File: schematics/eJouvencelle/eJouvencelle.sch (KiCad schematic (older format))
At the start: 42 parts

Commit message: reorganise components
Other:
- moved on the sheet: BZ?, C?, J?, Q?, R?, SW?A, U?, Y?

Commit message: convert logic voltage use to 3.3V
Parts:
- removed U?: LM1117IMPX-5.0/NOPB, symbol Regulator_Linear:LM1117-5.0
- added U?: LM1117-3.3, symbol Regulator_Linear:LM1117-3.3
- R? (x7): value 270R -> 100R
- Y?: value 16MHz -> 8MHz
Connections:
- net GND: now also U?.1 (GND)
- net Vbatt: now also U?.3 (VI)
- net +3V3: now reaches J?.2 (Pin_2)
- net +3V3: now also C?.1, C?.1, C?.1, C?.1, C?.1, R?.2, SW?.7 (B), U?.16 (VDD), U?.18 (AVCC), U?.3 (~LT), U?.4 (VCC), U?.6 (VCC), U?.2 (VO)
- removed net +5V: C?.1, C?.1, C?.1, C?.1, C?.1, J?.3 (Pin_3), R?.2, SW?.7 (B), U?.16 (VDD), U?.18 (AVCC), U?.3 (~LT), U?.4 (VCC), U?.6 (VCC)
- no-connect marks 3 -> 11
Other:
- note added: "Voltage regulation (3.3V)"
- note removed: "Voltage regulation (5V)"
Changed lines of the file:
@@
 Sheet 1 1
 Title "eJouvencelle"
-Date "2020-04-04"
+Date "2020-10-03"
 Rev "v3.0"
 Comp ""
@@
 F 3 "" H 5200 5850 50  0001 C CNN
 	1    5200 5850
-	1    0    0    -1
-$EndComp
-$Comp
-L power:+5V #PWR?
-U 1 1 5E88AC5A
-P 5200 2450
-F 0 "#PWR?" H 5200 2300 50  0001 C CNN
-F 1 "+5V" H 5215 2623 50  0000 C CNN
-F 2 "" H 5200 2450 50  0001 C CNN
-F 3 "" H 5200 2450 50  0001 C CNN
-	1    5200 2450
 	1    0    0    -1
 $EndComp
@@
 Connection ~ 5950 2850
 $Comp
-L power:+5V #PWR?
-U 1 1 5E8E172E
-P 2900 3600
-F 0 "#PWR?" H 2900 3450 50  0001 C CNN
-F 1 "+5V" H 2915 3773 50  0000 C CNN
-F 2 "" H 2900 3600 50  0001 C CNN
-F 3 "" H 2900 3600 50  0001 C CNN
-	1    2900 3600
-	1    0    0    -1
-$EndComp
-$Comp
 L power:GND #PWR?
 U 1 1 5E8E3004
@@
 Wire Wire Line
 	2300 3900 2300 4100
-$Comp
-L Regulator_Linear:LM1117-5.0 U?
-U 1 1 5E8E0075
-P 2300 3600
-F 0 "U?" H 2300 3842 50  0000 C CNN
-F 1 "LM1117IMPX-5.0/NOPB" H 2300 3751 50  0000 C CNN
-F 2 "" H 2300 3600 50  0001 C CNN
-F 3 "http://www.ti.com/lit/ds/symlink/lm1117.pdf" H 2300 3600 50  0001 C CNN
-	1    2300 3600
-	1    0    0    -1
-$EndComp
 Text GLabel 1750 3600 0    50   Input ~ 0
 Vbatt
@@
 	1900 4100 2300 4100
 Text Notes 1400 4500 0    50   ~ 0
-Voltage regulation (5V)
+Voltage regulation (3.3V)
 Wire Wire Line
 	2650 3600 2900 3600
@@
 P 4250 4300
 F 0 "Y?" H 4250 4525 50  0000 C CNN
-F 1 "16MHz" H 4250 4434 50  0000 C CNN
+F 1 "8MHz" H 4250 4434 50  0000 C CNN
 F 2 "" H 4250 4300 50  0001 C CNN
 F 3 "~" H 4250 4300 50  0001 C CNN
@@
 $EndComp
 $Comp
-L power:+5V #PWR?
-U 1 1 5E88FEF1
-P 8550 1200
-F 0 "#PWR?" H 8550 1050 50  0001 C CNN
-F 1 "+5V" H 8565 1373 50  0000 C CNN
-F 2 "" H 8550 1200 50  0001 C CNN
-F 3 "" H 8550 1200 50  0001 C CNN
-	1    8550 1200
-	1    0    0    -1
-$EndComp
-$Comp
 L power:GND #PWR?
 U 1 1 5E890F98
@@
 	8550 1250 8550 1450
 $Comp
-L power:+5V #PWR?
-U 1 1 5E89B064
-P 8000 1450
-F 0 "#PWR?" H 8000 1300 50  0001 C CNN
-F 1 "+5V" H 8015 1623 50  0000 C CNN
-F 2 "" H 8000 1450 50  0001 C CNN
-F 3 "" H 8000 1450 50  0001 C CNN
-	1    8000 1450
-	1    0    0    -1
-$EndComp
-$Comp
 L Device:R R?
 U 1 1 5E8C3C3B
 P 9450 1750
 F 0 "R?" V 9400 1850 50  0000 L CNN
-F 1 "270R" V 9400 1450 50  0000 L CNN
+F 1 "100R" V 9400 1450 50  0000 L CNN
 F 2 "" V 9380 1750 50  0001 C CNN
 F 3 "~" H 9450 1750 50  0001 C CNN
@@
 P 9450 1850
 F 0 "R?" V 9400 1950 50  0000 L CNN
-F 1 "270R" V 9400 1550 50  0000 L CNN
+F 1 "100R" V 9400 1550 50  0000 L CNN
 F 2 "" V 9380 1850 50  0001 C CNN
 F 3 "~" H 9450 1850 50  0001 C CNN
@@
 P 9450 1950
 F 0 "R?" V 9400 2050 50  0000 L CNN
-F 1 "270R" V 9400 1650 50  0000 L CNN
+F 1 "100R" V 9400 1650 50  0000 L CNN
 F 2 "" V 9380 1950 50  0001 C CNN
 F 3 "~" H 9450 1950 50  0001 C CNN
@@
 P 9450 2050
 F 0 "R?" V 9400 2150 50  0000 L CNN
-F 1 "270R" V 9400 1750 50  0000 L CNN
+F 1 "100R" V 9400 1750 50  0000 L CNN
 F 2 "" V 9380 2050 50  0001 C CNN
 F 3 "~" H 9450 2050 50  0001 C CNN
@@
 P 9450 2150
 F 0 "R?" V 9400 2250 50  0000 L CNN
-F 1 "270R" V 9400 1850 50  0000 L CNN
+F 1 "100R" V 9400 1850 50  0000 L CNN
 F 2 "" V 9380 2150 50  0001 C CNN
 F 3 "~" H 9450 2150 50  0001 C CNN
@@
 P 9450 2250
 F 0 "R?" V 9400 2350 50  0000 L CNN
-F 1 "270R" V 9400 1950 50  0000 L CNN
+F 1 "100R" V 9400 1950 50  0000 L CNN
 F 2 "" V 9380 2250 50  0001 C CNN
 F 3 "~" H 9450 2250 50  0001 C CNN
@@
 P 9450 2350
 F 0 "R?" V 9400 2450 50  0000 L CNN
-F 1 "270R" V 9400 2050 50  0000 L CNN
+F 1 "100R" V 9400 2050 50  0000 L CNN
 F 2 "" V 9380 2350 50  0001 C CNN
 F 3 "~" H 9450 2350 50  0001 C CNN
@@
 	9650 4000 9650 4050
 $Comp
-L power:+5V #PWR?
-U 1 1 5E933D66
-P 9650 3700
-F 0 "#PWR?" H 9650 3550 50  0001 C CNN
-F 1 "+5V" H 9665 3873 50  0000 C CNN
-F 2 "" H 9650 3700 50  0001 C CNN
-F 3 "" H 9650 3700 50  0001 C CNN
-	1    9650 3700
-	-1   0    0    -1
-$EndComp
-$Comp
 L Device:R R?
 U 1 1 5E9329C4
@@
 Wire Wire Line
 	10150 4250 10300 4250
-Wire Wire Line
-	10000 4450 10300 4450
-Wire Wire Line
-	10000 4500 10000 4450
 Wire Wire Line
 	10200 4650 10300 4650
@@
 $EndComp
 $Comp
-L power:+5V #PWR?
-U 1 1 5E917405
-P 10000 4500
-F 0 "#PWR?" H 10000 4350 50  0001 C CNN
-F 1 "+5V" H 10015 4673 50  0000 C CNN
-F 2 "" H 10000 4500 50  0001 C CNN
-F 3 "" H 10000 4500 50  0001 C CNN
-	1    10000 4500
-	1    0    0    1
-$EndComp
-NoConn ~ 10300 4550
-$Comp
 L power:GND #PWR?
 U 1 1 5E9155DD
@@
 Wire Wire Line
 	2000 1500 2000 1550
-$Comp
-L power:+5V #PWR?
-U 1 1 5E8B2017
-P 2000 1500
-F 0 "#PWR?" H 2000 1350 50  0001 C CNN
-F 1 "+5V" H 2015 1673 50  0000 C CNN
-F 2 "" H 2000 1500 50  0001 C CNN
-F 3 "" H 2000 1500 50  0001 C CNN
-	1    2000 1500
-	1    0    0    -1
-$EndComp
 Connection ~ 2750 1000
 Wire Wire Line
@@
 Wire Wire Line
 	5800 3700 7550 3700
+$Comp
+L power:+3V3 #PWR?
+U 1 1 5F79539F
+P 2900 3600
+F 0 "#PWR?" H 2900 3450 50  0001 C CNN
+F 1 "+3V3" H 2915 3773 50  0000 C CNN
+F 2 "" H 2900 3600 50  0001 C CNN
+F 3 "" H 2900 3600 50  0001 C CNN
+	1    2900 3600
+	1    0    0    -1
+$EndComp
+$Comp
+L power:+3V3 #PWR?
+U 1 1 5F795FB2
+P 2000 1500
+F 0 "#PWR?" H 2000 1350 50  0001 C CNN
+F 1 "+3V3" H 2015 1673 50  0000 C CNN
+F 2 "" H 2000 1500 50  0001 C CNN
+F 3 "" H 2000 1500 50  0001 C CNN
+	1    2000 1500
+	1    0    0    -1
+$EndComp
+$Comp
+L power:+3V3 #PWR?
+U 1 1 5F797225
+P 5200 2450
+F 0 "#PWR?" H 5200 2300 50  0001 C CNN
+F 1 "+3V3" H 5215 2623 50  0000 C CNN
+F 2 "" H 5200 2450 50  0001 C CNN
+F 3 "" H 5200 2450 50  0001 C CNN
+	1    5200 2450
+	1    0    0    -1
+$EndComp
+$Comp
+L power:+3V3 #PWR?
+U 1 1 5F7984BD
+P 8550 1200
+F 0 "#PWR?" H 8550 1050 50  0001 C CNN
+F 1 "+3V3" H 8565 1373 50  0000 C CNN
+F 2 "" H 8550 1200 50  0001 C CNN
+F 3 "" H 8550 1200 50  0001 C CNN
+	1    8550 1200
+	1    0    0    -1
+$EndComp
+$Comp
+L power:+3V3 #PWR?
+U 1 1 5F799711
+P 8000 1450
+F 0 "#PWR?" H 8000 1300 50  0001 C CNN
+F 1 "+3V3" H 8015 1623 50  0000 C CNN
+F 2 "" H 8000 1450 50  0001 C CNN
+F 3 "" H 8000 1450 50  0001 C CNN
+	1    8000 1450
+	1    0    0    -1
+$EndComp
+$Comp
+L power:+3V3 #PWR?
+U 1 1 5F79A562
+P 9650 3700
+F 0 "#PWR?" H 9650 3550 50  0001 C CNN
+F 1 "+3V3" H 9665 3873 50  0000 C CNN
+F 2 "" H 9650 3700 50  0001 C CNN
+F 3 "" H 9650 3700 50  0001 C CNN
+	1    9650 3700
+	1    0    0    -1
+$EndComp
+$Comp
+L power:+3V3 #PWR?
+U 1 1 5F7ACFC0
+P 10050 4600
+F 0 "#PWR?" H 10050 4450 50  0001 C CNN
+F 1 "+3V3" H 10065 4773 50  0000 C CNN
+F 2 "" H 10050 4600 50  0001 C CNN
+F 3 "" H 10050 4600 50  0001 C CNN
+	1    10050 4600
+	-1   0    0    1
+$EndComp
+Wire Wire Line
+	10300 4550 10050 4550
+Wire Wire Line
+	10050 4550 10050 4600
+NoConn ~ 10300 4450
+NoConn ~ 4600 3350
+NoConn ~ 4600 3450
+NoConn ~ 4600 5350
+NoConn ~ 4600 5450
+NoConn ~ 4600 5550
+NoConn ~ 5800 5350
+NoConn ~ 5800 5450
+NoConn ~ 5800 5550
+$Comp
+L Regulator_Linear:LM1117-3.3 U?
+U 1 1 5F81B759
+P 2300 3600
+F 0 "U?" H 2300 3842 50  0000 C CNN
+F 1 "LM1117-3.3" H 2300 3751 50  0000 C CNN
+F 2 "" H 2300 3600 50  0001 C CNN
+F 3 "http://www.ti.com/lit/ds/symlink/lm1117.pdf" H 2300 3600 50  0001 C CNN
+	1    2300 3600
+	1    0    0    -1
+$EndComp
 $EndSCHEMATC

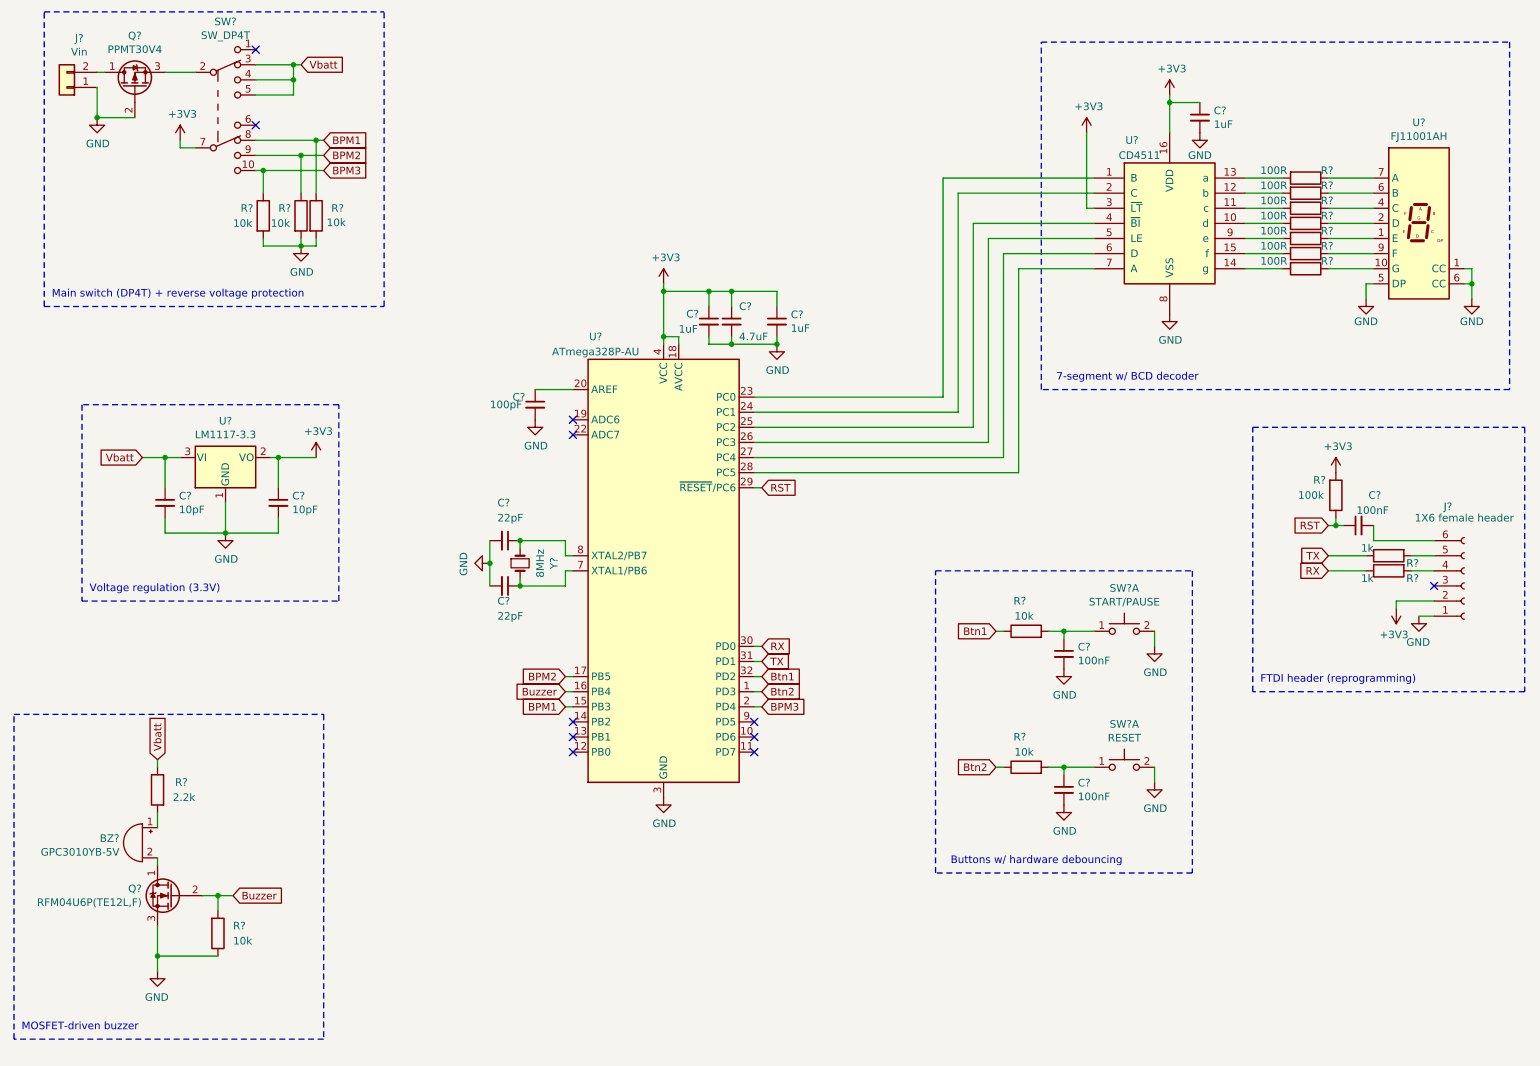
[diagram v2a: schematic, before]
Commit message: replace voltage regulator by buck converter + change components placement
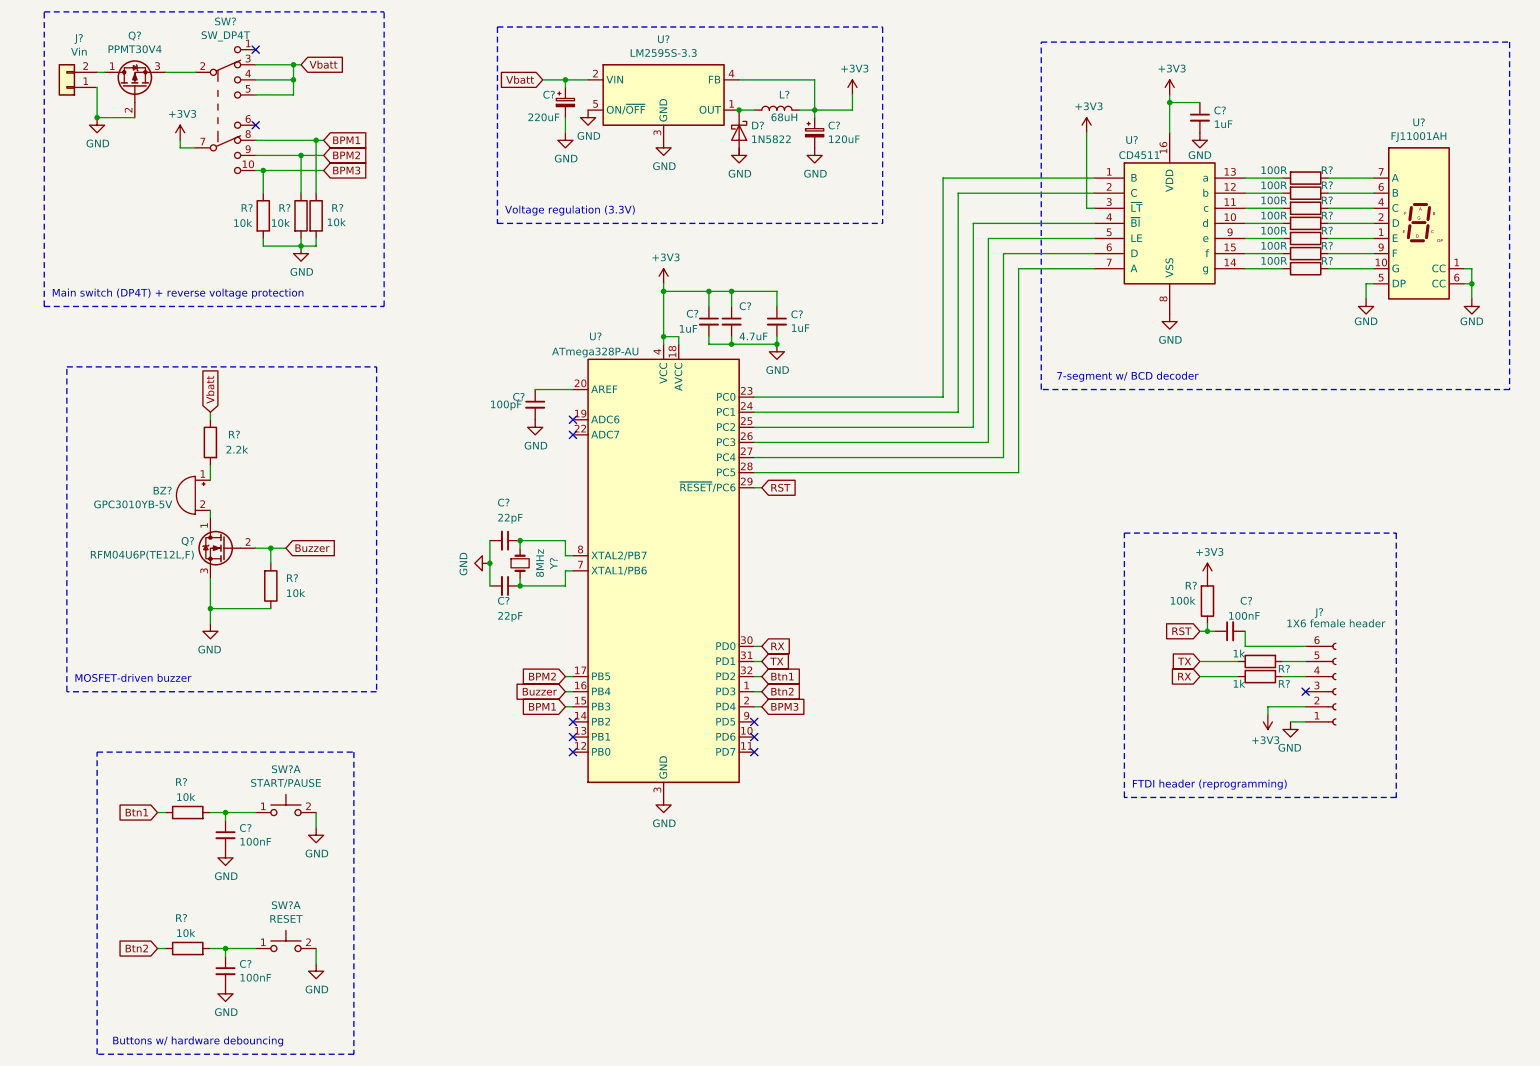
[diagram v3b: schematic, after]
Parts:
- removed C? (x2): 10pF, symbol Device:C_Small
- removed U?: LM1117-3.3, symbol Regulator_Linear:LM1117-3.3
- added C?: 220uF, symbol Device:CP_Small
- added C?: 120uF, symbol Device:CP_Small
- added D?: 1N5822, Diode_THT:D_DO-201AD_P15.24mm_Horizontal, symbol Diode:1N5822
- added L?: 68uH, symbol Device:L
- added U?: LM2595S-3.3, Package_TO_SOT_SMD:TO-263-5_TabPin3, symbol Regulator_Switching:LM2595S-3.3
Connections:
- net +3V3: now also C?.1, L?.2, U?.4 (FB)
- net GND: now also C?.2, C?.2, U?.3 (GND), U?.5 (ON/~OFF)
- net Vbatt: now also C?.1, U?.2 (VIN)
- new net: D?.1 (K), L?.1, U?.1 (OUT)
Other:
- moved on the sheet: BZ?, C?, J?, Q?, R?, SW?A
